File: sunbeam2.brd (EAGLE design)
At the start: 120 x 95 mm, 286 parts, among them IC10 LM1117IMPX-3.3, IC2 A4983, IC3 A4983, IC4 A4983, IC5 A4983, IC6 A4983, IC7 FT232RLSSOP, IC8 LM2675, IC9 LMV358MMX, Q1 BC857ALT1SMD, Q2 IRLHM630TR2PBF, Q3 IRLHM630TR2PBF, Q4 IRLHM630TR2PBF, T2 bc848, T3 bc858, T4 bc848, T5 bc858, T6 bc848, T7 bc858, U2 USD-SOCKETNEW

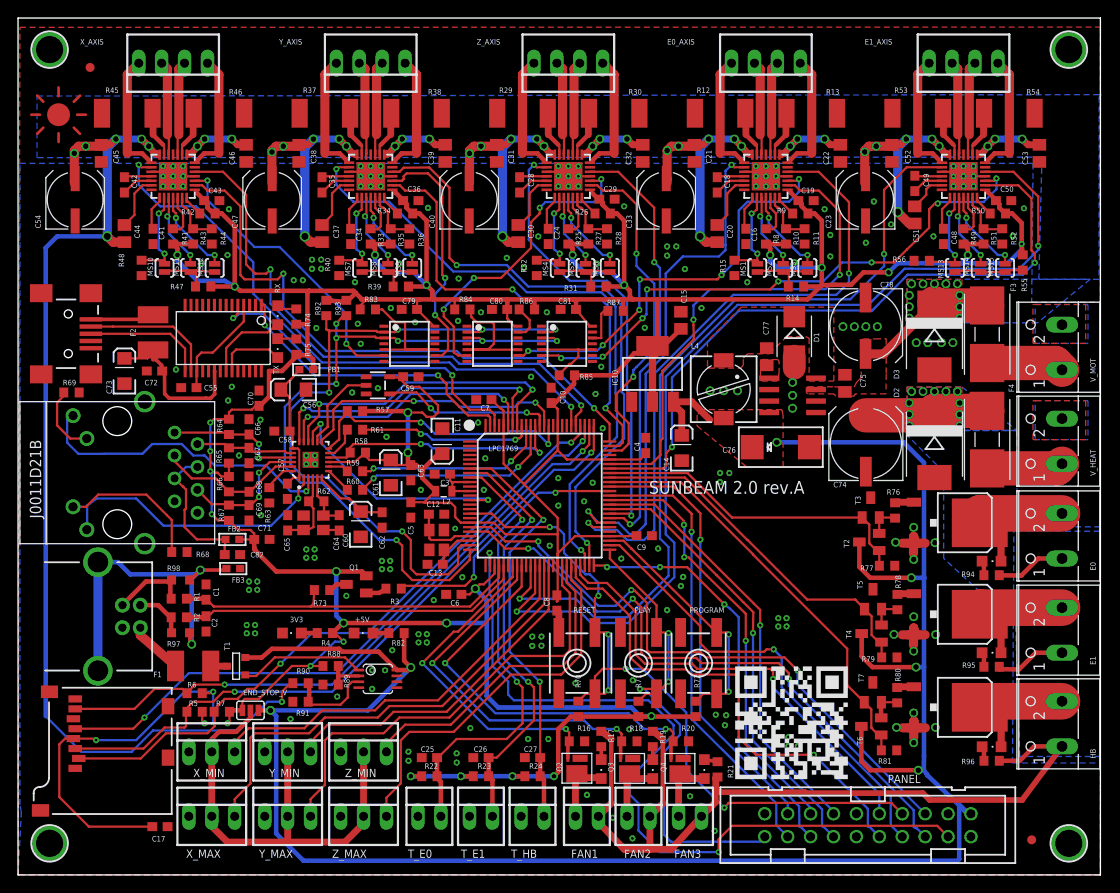
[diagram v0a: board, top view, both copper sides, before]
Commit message: -changed 3 2 channel pots to one 6 channel -moved play button -added fet driver for heater instead of bjts -changed some polygons [thanks triffin_hunter]
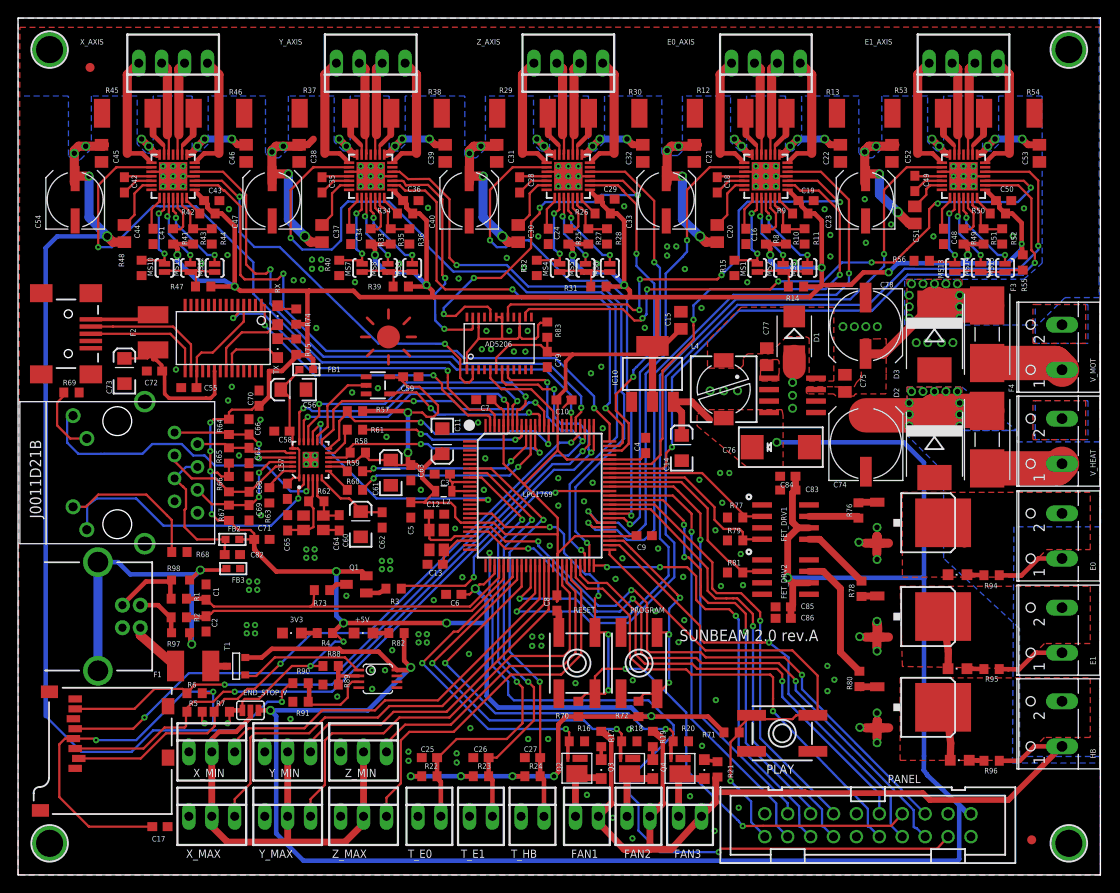
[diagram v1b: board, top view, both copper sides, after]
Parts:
- removed C80, C81: 0.1uF, rcl:C0603
- removed R84, R85: 15K, rcl:R0603
- removed R86, R87, R92, R93: 10K, rcl:R0603
- removed T2, T4, T6: bc848, transistor-neu-to92:SOT23-BEC
- removed T3, T5, T7: bc858, transistor-neu-to92:SOT23-BEC
- removed U$13, U$14, U$15: MCP4631, microchip:TSSOP14
- removed U$24: IRLR8743, transistor-power:D-PAK_TO252AA
- added AD5206: AD5206, analog-devices:TSSOP24
- added C83, C84: 0.1uF, rcl:C0603
- added C85, C86: 4.7uF, rcl:C0603
- added E0_FET: IRLR8743, transistor-power:D-PAK_TO252AA
- added FET_DRV1, FET_DRV2: TC4427, custom_esorensen:SOIC8
- R76, R78, R80: value 1K -> 22R
- R77, R79, R81: value 1K -> 10K
- R83: value 15K -> 10K
- moved U$21 44.1 mm to (41.1, 59.6)
- moved R81 26.1 mm to (79.5, 33.5), turned to 180 degrees
- moved R79 21.5 mm to (79.5, 37.1), turned to 180 degrees
- moved R83 20.0 mm to (58.7, 60.5), turned to 270 degrees
- moved PLAY 17.7 mm to (84.7, 15.7), turned to 180 degrees
- moved R77 17.7 mm to (79.5, 39.6), turned to 180 degrees
- moved C79 16.3 mm to (58.7, 57.1), turned to 270 degrees
- moved R71 10.6 mm to (79.1, 15.8), turned to 180 degrees
- moved PROGRAM 6.60 mm to (68.8, 23.5)
- moved R72 6.35 mm to (68.8, 18.4)
- moved R80 4.56 mm to (93.3, 21.7), turned to 90 degrees
- moved R78 4.24 mm to (93.5, 31.7), turned to 90 degrees
- moved LED7 4.17 mm to (104.2, 22.9), turned to 90 degrees
- moved E1_FET 4.07 mm to (100.1, 28.6)
- moved HOTBET_FET 4.06 mm to (100.1, 18.6)
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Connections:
- removed net N$141: LPC1769.85
- removed net N$161: R83.1, U$13.10, U$13.5
- removed net N$162: R84.1, U$14.10, U$14.5
- removed net N$163: R85.1, U$15.10, U$15.5
- removed net N$167: U$15.9
- removed net N$168: R86.1, U$14.13
- removed net N$170: R87.1, U$15.12
- new net N$148: AD5206.1, AD5206.15, AD5206.18, AD5206.19, AD5206.22, R83.1
- new net POT_CS: AD5206.5, LPC1769.85
- net +3V3: now also AD5206.6, C79.1; no longer C79.2, C80.2, C81.2, R84.2, R85.2, R86.2, R87.2, R92.2, R93.2, U$13.14, U$14.14, U$15.14
- net 5V: now also C83.1, C84.1, C85.1, C86.1, FET_DRV1.6, FET_DRV2.6; no longer T2.C, T4.C, T6.C
- net E0_H: now also FET_DRV1.2; no longer T2.B, T3.B
- net E1_H: now also FET_DRV1.4; no longer T4.B, T5.B
- net GND: now also AD5206.13, AD5206.16, AD5206.21, AD5206.24, AD5206.3, AD5206.4, AD5206.9, C79.2, C83.2, C84.2, C85.2, C86.2, E0_FET.3, FET_DRV1.3, FET_DRV2.3; no longer C79.1, C80.1, C81.1, T3.C, T5.C, T7.C, U$13.1, U$13.12, U$13.13, U$13.4, U$13.7, U$13.8, U$14.1, U$14.12, U$14.4, U$14.7, U$14.8, U$15.1, U$15.13, U$15.4, U$15.7, U$15.8, U$24.3
- net HB_H: now also FET_DRV2.2; no longer T6.B, T7.B
- net N$135: now also FET_DRV1.5, R78.2; no longer R76.2, T2.E, T3.E
- net N$139: now also FET_DRV2.7; no longer T6.E, T7.E
- net N$30: now also E0_FET.4; no longer U$24.4
- net N$31: now also E0_FET.1; no longer U$24.1
- net N$33: now also FET_DRV1.7, R76.2; no longer R78.2, T4.E, T5.E
- net POT_SCL: no longer R92.1, U$13.2, U$14.2, U$15.2
- net POT_SDA: no longer R93.1, U$13.3, U$14.3, U$15.3
- net REF_E0: now also AD5206.17; no longer U$14.9
- net REF_E1: now also AD5206.14; no longer U$15.6
- net REF_X: now also AD5206.2; no longer U$13.6
- net REF_Y: now also AD5206.23; no longer U$13.9
- net REF_Z: now also AD5206.20; no longer U$14.6
- net SD_MOSI: now also AD5206.7
- net SD_SCK: now also AD5206.8
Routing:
- net POT_SDA: track 79.4 -> 0.00 mm, vias 7 -> 0
- net POT_SCL: track 77.8 -> 0.00 mm, vias 5 -> 0
- net +12V: track 288.8 -> 258.9 mm
- net HB_H: track 48.3 -> 23.2 mm
- net N$148: track 0.00 -> 22.0 mm
- net E1_H: track 40.9 -> 21.2 mm
- net ENABLE_Y: track 71.9 -> 90.6 mm
- net E0_H: track 36.9 -> 19.2 mm
- net SD_MOSI: track 75.3 -> 92.6 mm, vias 2 -> 3
- net ENABLE_X: track 66.0 -> 82.0 mm
- net N$161: track 15.8 -> 0.00 mm
- net N$162: track 14.8 -> 0.00 mm
- net SD_SCK: track 71.3 -> 85.6 mm, vias 2 -> 3
- net REF_X: track 32.3 -> 44.7 mm
- net N$30: track 15.4 -> 3.34 mm
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- added copper zone on layer 1, net N$28
- added copper zone on layer 1, net N$29
- added copper zone on layer 1, net N$30

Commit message: -changed heaters fuse -some slight component changes
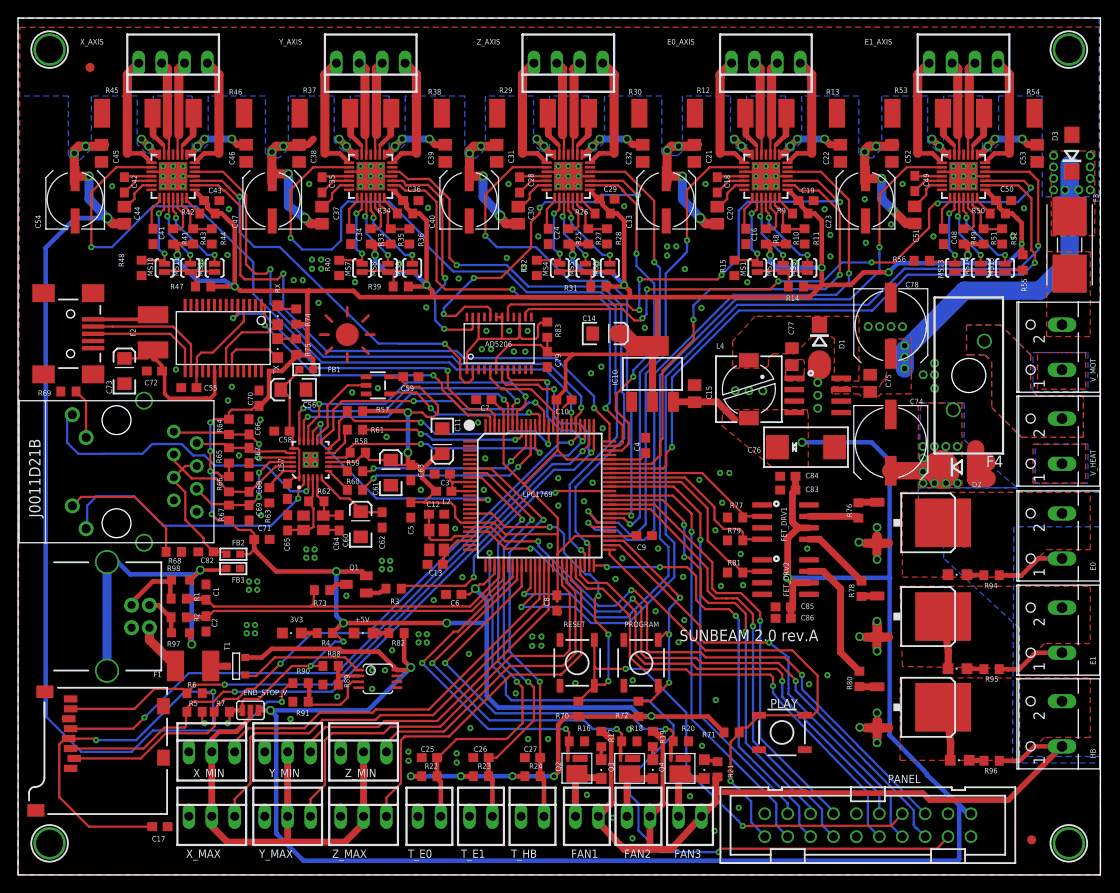
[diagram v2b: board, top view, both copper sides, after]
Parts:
- removed U$5: ETHERNET, con-j0011d21b-v3:J0011D21B
- added RJ1: ETHERNET, con-j0011d21b-v3:J0011D21B
- C15: value 1uF -> 0.1uF
- C23, C33, C40, C47, C54: value (none) -> 100uF
- D1: value 10BQ040PBF -> SS14; device diode:SMB -> diode:DO214AC
- D2, D3: value (none) -> M4; device diode:SMC -> diode:DO214AC
- F4: value SMF_OMNIBLOK_154.062 -> 01530008Z; device _hhn_littlefuse_Nano2SMF_2:NANO2_SMF_FUSEBLOCK -> Littelfuse_By_element14_Batch_1:01530008Z
- L2: device SparkFun:0805 -> SparkFun:0603
- PLAY, PROGRAM, RESET: device microbuilder:EVQ-Q2 -> SparkFun:TACTILE_SWITCH_SMD
- R11, R28, R36, R44, R52: value R40 -> 10K
- R12, R13, R29, R30, R37, R38, R45, R46, R53, R54: value 0.2R -> 0.5R
- R3: value 50R -> 470R
- R90: value 5K -> 4K7
- T1: value (none) -> IRLML2246TRPBF
- moved D3 25.4 mm to (116.8, 80.0), turned to 90 degrees
- moved C14 15.3 mm to (65.1, 60.0), turned to 0 degrees
- moved F3 13.5 mm to (116.6, 69.8)
- moved C15 8.27 mm to (75.0, 53.4)
- moved F4 7.40 mm to (105.4, 55.4), turned to 180 degrees
- moved U$21 4.58 mm to (36.5, 59.9)
- moved D2 3.78 mm to (104.4, 45.2), turned to 0 degrees
- moved C82 2.95 mm to (20.8, 35.8), turned to 180 degrees
- moved D1 2.90 mm to (88.9, 58.9)
- moved C75 2.79 mm to (94.5, 54.5)
- moved C76 2.79 mm to (87.4, 47.4)
- moved IC8 2.79 mm to (88.7, 53.2)
- moved C77 2.79 mm to (85.8, 57.5)
- moved C78 2.79 mm to (96.8, 60.9)
- moved L4 2.79 mm to (81.0, 53.8)
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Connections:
- removed net N$118: C67.1, R65.2, U$5.TD-, U3.20
- removed net N$127: C69.1, R67.2, U$5.RD-, U3.22
- removed net N$128: C68.1, R66.2, U$5.RD+, U3.23
- removed net N$146: F3.1, V_MOT.1
- new net N$141: C69.1, R67.2, RJ1.RD-, U3.22
- new net N$149: R68.1, RJ1.Y_GND
- new net N$150: R69.1, RJ1.G_GND
- new net N$151: C82.1, FB2.2, RJ1.CT, RJ1.CT2
- net +3V3: now also C14.A; no longer C15.1
- net 5V: now also C15.1; no longer C14.A
- net GND: now also PLAY.3, PLAY.4, PROGRAM.3, PROGRAM.4, RESET.3, RESET.4, RJ1.CHS1, RJ1.CHS2, RJ1.GND, RJ1.NC, V_HEAT.1, V_MOT.1; no longer PLAY.B, PLAY.B', PROGRAM.B, PROGRAM.B', RESET.B, RESET.B', U$5.CHS1, U$5.CHS2, U$5.GND, U$5.NC, V_HEAT.2, V_MOT.2
- net LED1/REGOFF: now also RJ1.G; no longer U$5.G
- net LED2/NINTSEL: now also RJ1.Y; no longer U$5.Y
- net N$117: now also F4.P$1, V_HEAT.2; no longer C66.1, R64.2, U$5.TD+, U3.21
- net N$129: now also C66.1, R64.2, RJ1.TD+, U3.21; no longer R68.1, U$5.Y_GND
- net N$132: now also C67.1, R65.2, RJ1.TD-, U3.20; no longer R69.1, U$5.G_GND
- net N$145: now also C68.1, R66.2, RJ1.RD+, U3.23; no longer C82.1, FB2.2, U$5.CT, U$5.CT2
- net N$27: now also F3.1, V_MOT.2; no longer F4.1, V_HEAT.1
- net PLAY: now also PLAY.1, PLAY.2; no longer PLAY.A, PLAY.A'
- net PROGRAM: now also PROGRAM.1, PROGRAM.2; no longer PROGRAM.A, PROGRAM.A'
- net RESET: now also RESET.1, RESET.2; no longer RESET.A, RESET.A'
- net V_EXTR: now also F4.P$2; no longer F4.2
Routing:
- net N$128: track 16.3 -> 0.00 mm
- net N$117: track 15.2 -> 0.00 mm, vias 2 -> 0
- net N$141: track 0.00 -> 15.0 mm, vias 0 -> 2
- net N$127: track 14.9 -> 0.00 mm, vias 2 -> 0
- net N$149: track 0.00 -> 14.9 mm
- net N$151: track 0.00 -> 14.7 mm
- net N$118: track 11.2 -> 0.00 mm
- net +12V: track 258.9 -> 269.9 mm, vias 57 -> 59
- net V_EXTR: track 122.4 -> 113.3 mm, vias 11 -> 10
- net 5V: track 242.3 -> 233.2 mm
- net N$146: track 8.61 -> 0.00 mm
- net N$27: track 8.52 -> 0.00 mm
- net N$150: track 0.00 -> 5.56 mm
- net N$132: track 7.88 -> 11.3 mm
- net +3V3: track 618.0 -> 620.0 mm
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- added copper zone on layer 1, net N$117
- added copper zone on layer 16, net N$117
- added copper zone on layer 1, net N$27
